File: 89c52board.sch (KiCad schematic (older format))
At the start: 46 parts, among them J1 Anodes, J11 P0.6-7, J12 P1.4-7, J13 P3.6-7, J2 Anodes, J3 Cathodes, J4 RTC board, J5 ISP, J6 12VDC, Q1 NPN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

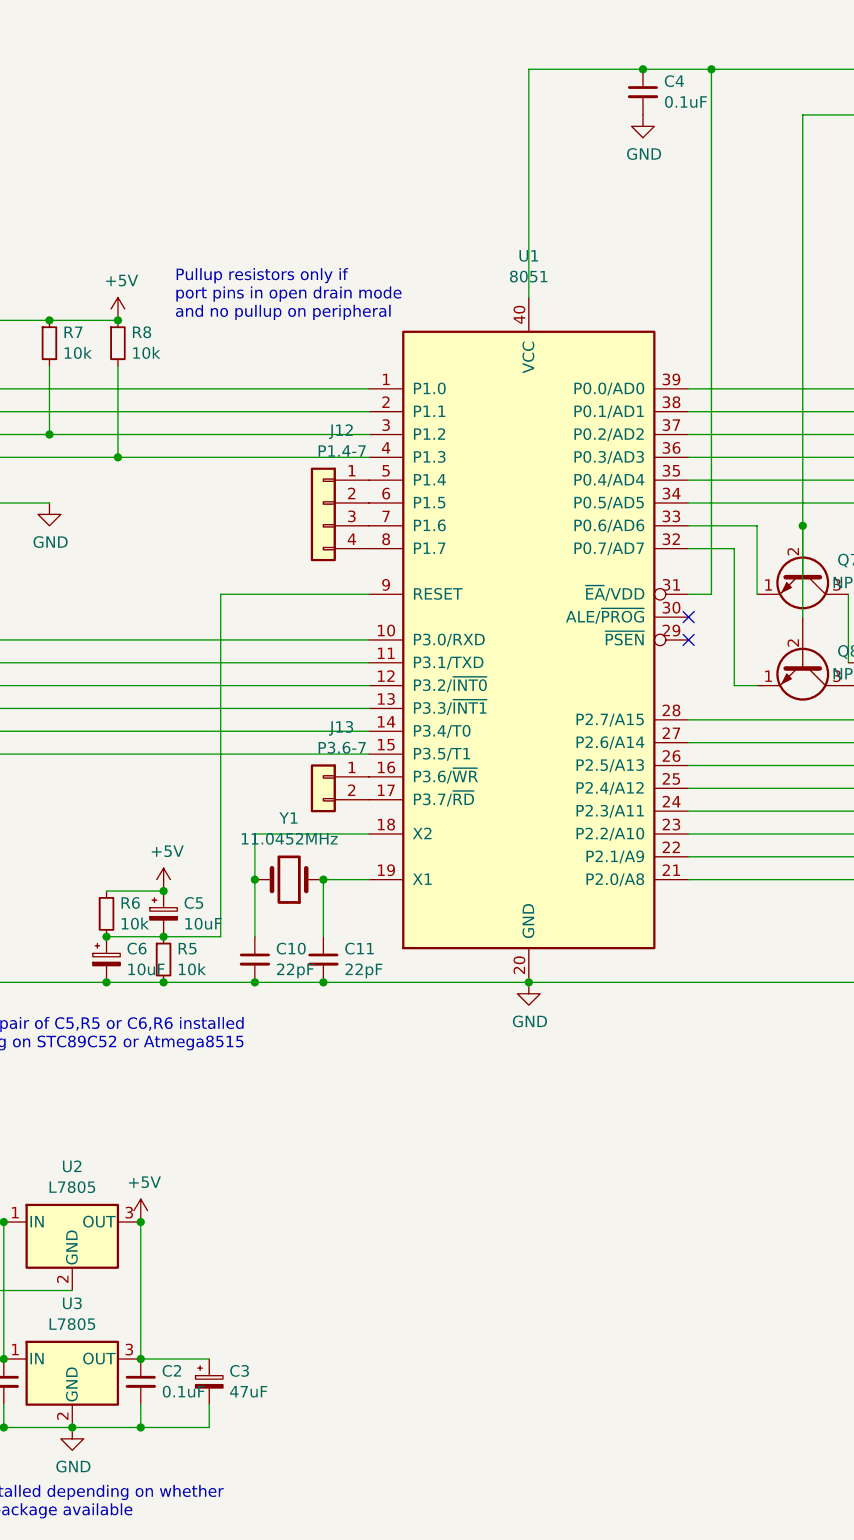
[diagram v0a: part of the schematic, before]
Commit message: Cosmetic: swap C2 and C4 labels to better reflect their positions on board
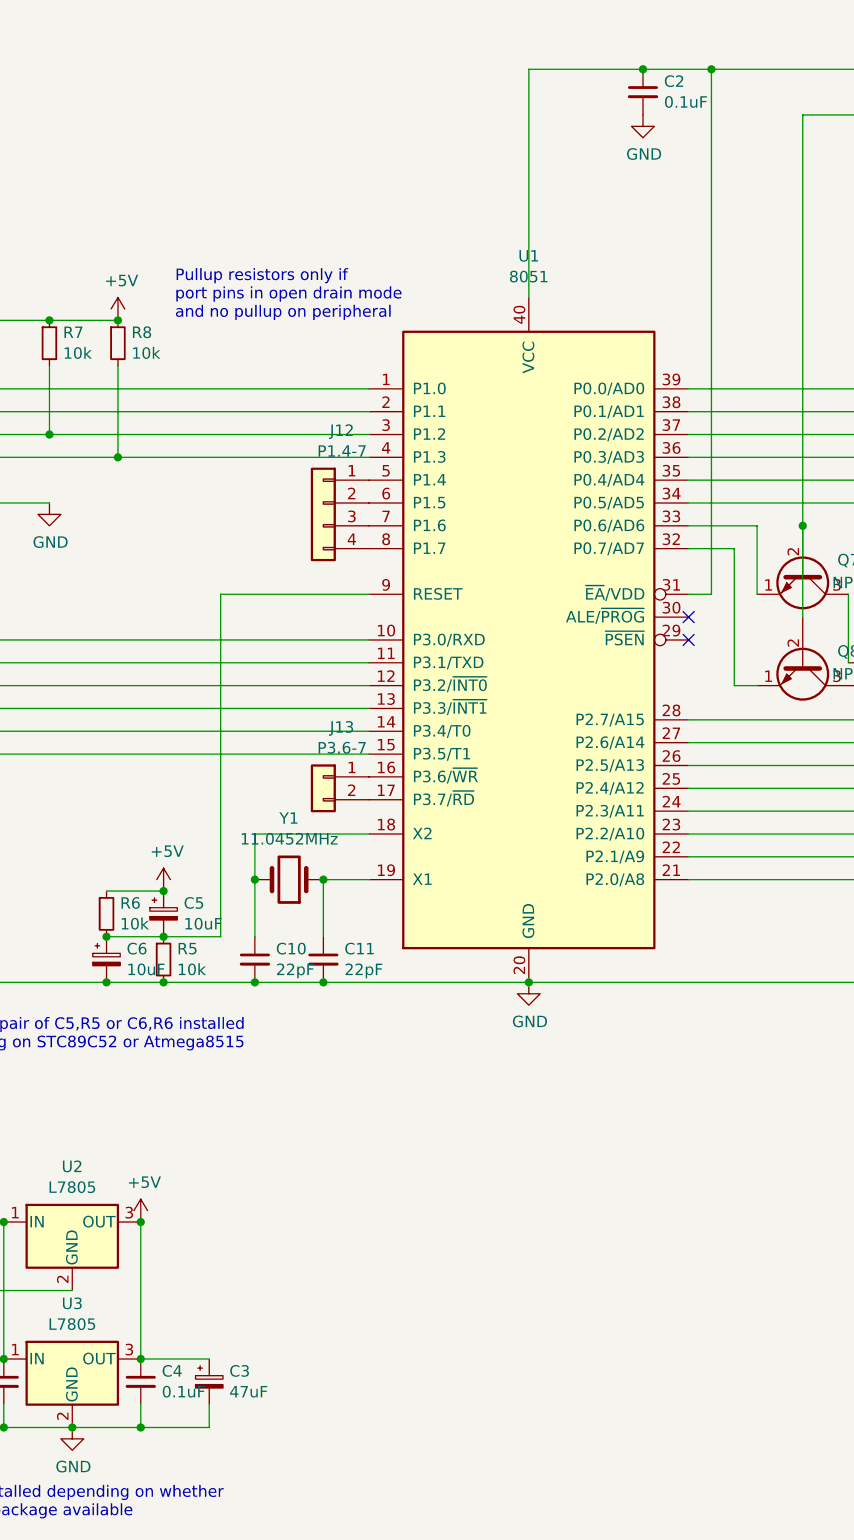
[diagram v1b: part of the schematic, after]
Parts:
- renumbered C4 to C2, C2 to C4
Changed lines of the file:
@@
 Connection ~ 7500 800
 $Comp
-L Device:C_Small C2
+L Device:C_Small C4
 U 1 1 5EF6793C
 P 3850 6550
-F 0 "C2" H 3942 6596 50  0000 L CNN
+F 0 "C4" H 3942 6596 50  0000 L CNN
 F 1 "0.1uF" H 3942 6505 50  0000 L CNN
 F 2 "Capacitor_THT:C_Disc_D3.8mm_W2.6mm_P2.50mm" H 3850 6550 50  0001 C CNN
@@
 	5550 800  6050 800
 $Comp
-L Device:C_Small C4
+L Device:C_Small C2
 U 1 1 5F443AD3
 P 6050 900
-F 0 "C4" H 6142 946 50  0000 L CNN
+F 0 "C2" H 6142 946 50  0000 L CNN
 F 1 "0.1uF" H 6142 855 50  0000 L CNN
 F 2 "Capacitor_THT:C_Disc_D3.8mm_W2.6mm_P2.50mm" H 6050 900 50  0001 C CNN

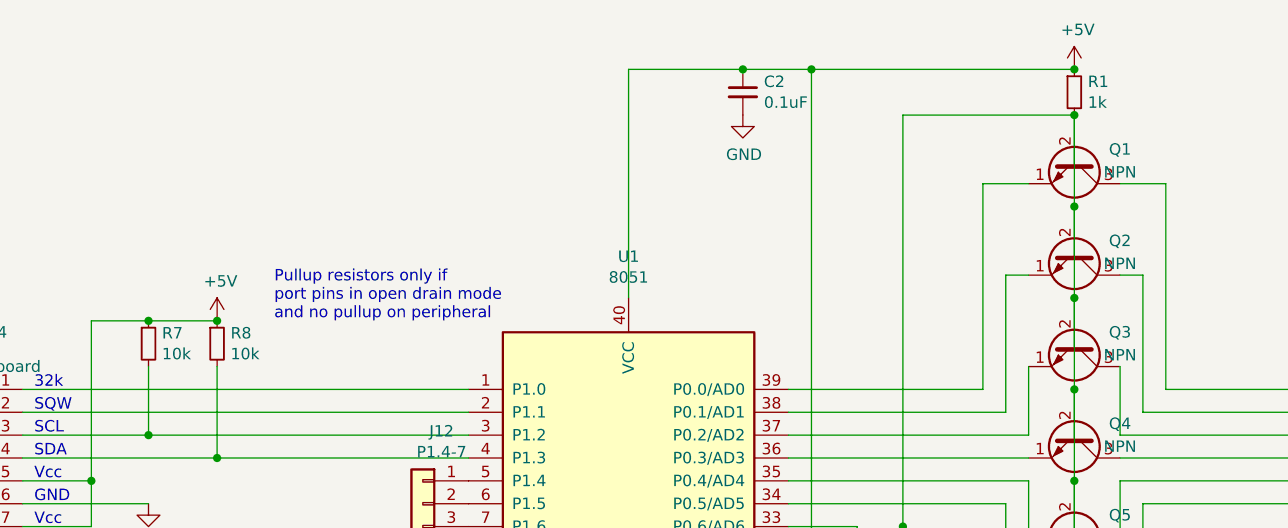
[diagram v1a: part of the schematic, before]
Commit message: More suitable values for I2C pullup resistors and digit driver transistor base resistor. Board unchanged
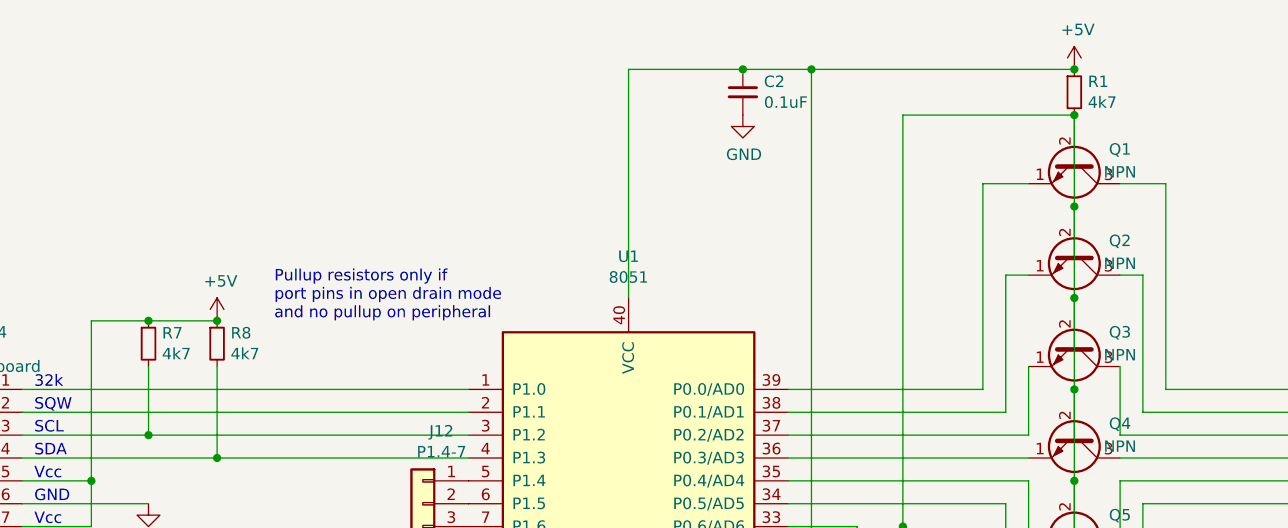
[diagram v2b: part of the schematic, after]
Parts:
- R1: value 1k -> 4k7
- R7, R8: value 10k -> 4k7
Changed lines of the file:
@@
 P 7500 900
 F 0 "R1" H 7559 946 50  0000 L CNN
-F 1 "1k" H 7559 855 50  0000 L CNN
+F 1 "4k7" H 7559 855 50  0000 L CNN
 F 2 "Resistor_THT:R_Axial_DIN0207_L6.3mm_D2.5mm_P10.16mm_Horizontal" H 7500 900 50  0001 C CNN
 F 3 "~" H 7500 900 50  0001 C CNN
@@
 P 3450 2000
 F 0 "R7" H 3509 2046 50  0000 L CNN
-F 1 "10k" H 3509 1955 50  0000 L CNN
+F 1 "4k7" H 3509 1955 50  0000 L CNN
 F 2 "Resistor_THT:R_Axial_DIN0207_L6.3mm_D2.5mm_P10.16mm_Horizontal" H 3450 2000 50  0001 C CNN
 F 3 "~" H 3450 2000 50  0001 C CNN
@@
 P 3750 2000
 F 0 "R8" H 3809 2046 50  0000 L CNN
-F 1 "10k" H 3809 1955 50  0000 L CNN
+F 1 "4k7" H 3809 1955 50  0000 L CNN
 F 2 "Resistor_THT:R_Axial_DIN0207_L6.3mm_D2.5mm_P10.16mm_Horizontal" H 3750 2000 50  0001 C CNN
 F 3 "~" H 3750 2000 50  0001 C CNN
